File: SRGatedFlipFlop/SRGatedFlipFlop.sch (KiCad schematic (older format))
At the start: 5 parts, among them U1 74LS08, U2 74LS08, U3 74LS02, U4 74LS04

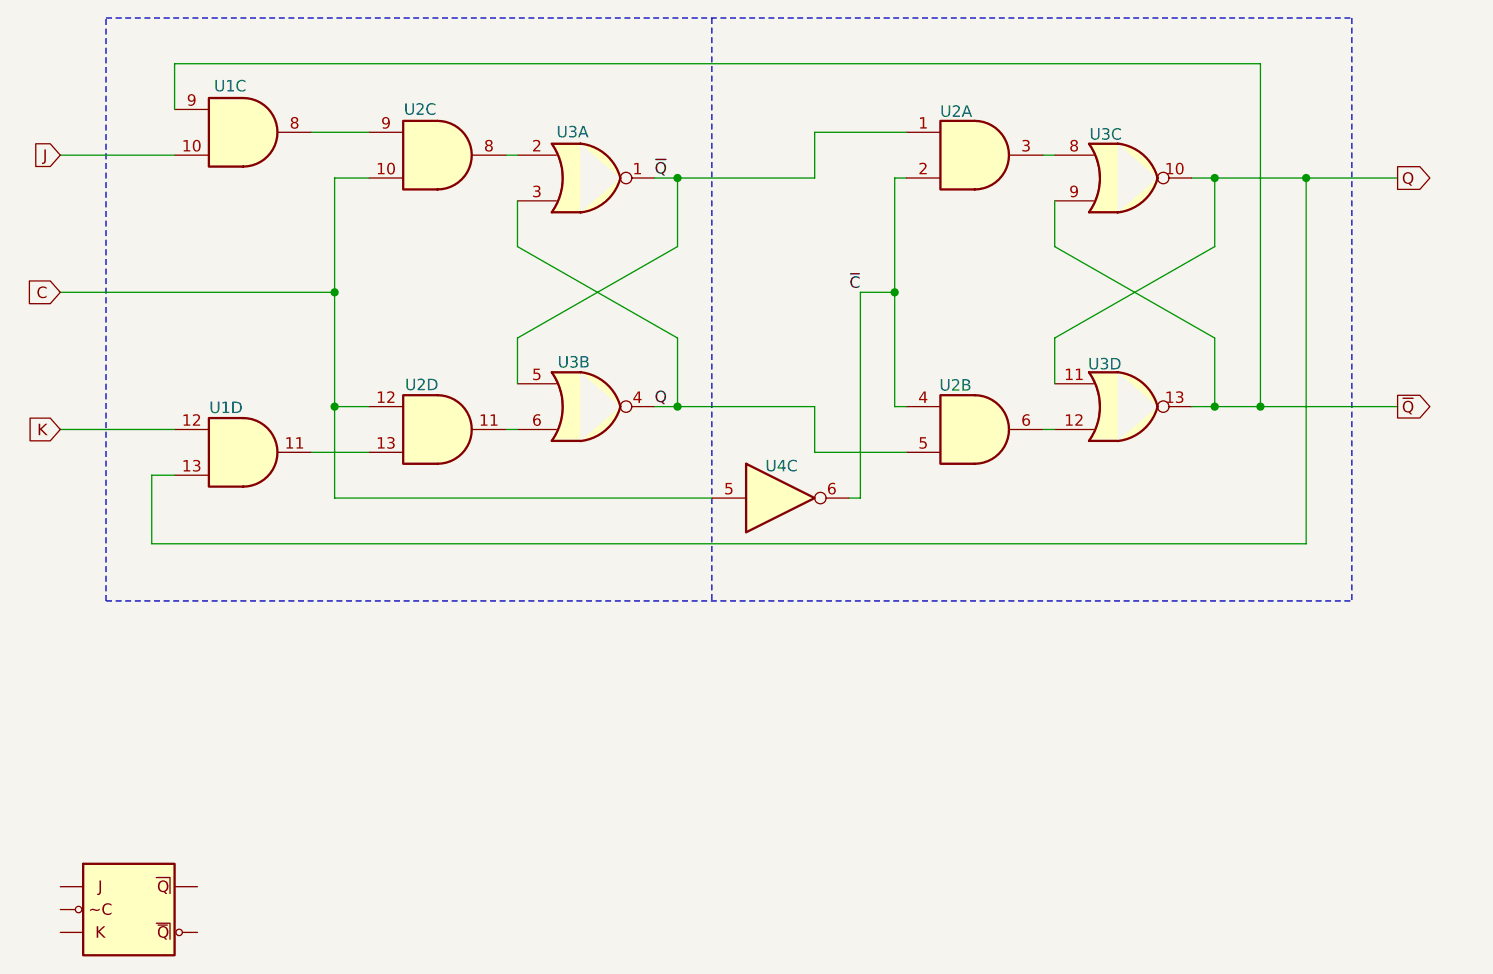
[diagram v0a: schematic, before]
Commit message: add gated S/R latch
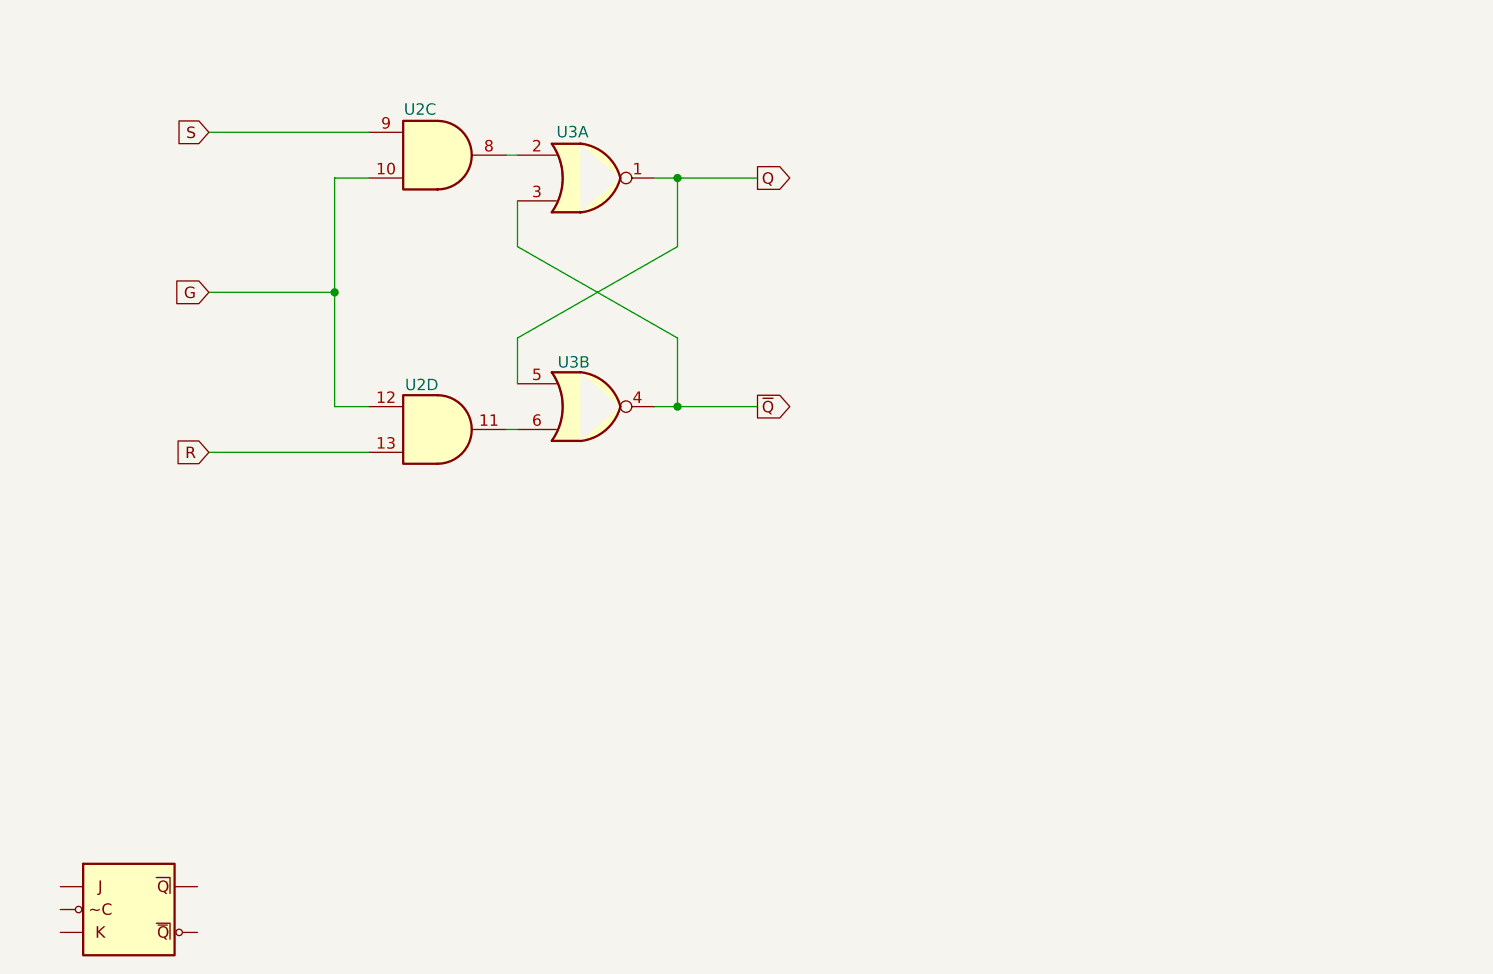
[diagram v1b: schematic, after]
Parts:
- removed U1: 74LS08, symbol 74xx:74LS08
- removed unit 2 of U2
- removed unit 1 of U2
- removed unit 4 of U3
- removed unit 3 of U3
- removed U4: 74LS04, symbol 74xx:74LS04
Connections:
- net Q: now also U3.1, U3.5; no longer U3.3, U3.4
- net ~Q: now also U3.3, U3.4; no longer U3.1, U3.5
- net S: now reaches U2.9
- net R: now reaches U2.13
- net C renamed G
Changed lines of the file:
@@
 EESchema Schematic File Version 4
-LIBS:FlipFlops-cache
+LIBS:SRGatedFlipFlop-cache
 EELAYER 30 0
 EELAYER END
@@
 Wire Wire Line
 	5650 3950 5650 4250
-Connection ~ 5650 4250
 Wire Wire Line
 	5650 3250 5650 3550
 Wire Wire Line
 	5650 3550 4950 3950
-Connection ~ 5650 3250
-Wire Wire Line
-	5650 3250 6250 3250
-$Comp
-L 74xx:74LS04 U4
-U 3 1 5F9C789E
-P 6100 4650
-F 0 "U4" H 6105 4790 50  0000 C CNN
-F 1 "74LS04" H 6100 4900 50  0001 C CNN
-F 2 "" H 6100 4650 50  0001 C CNN
-F 3 "http://www.ti.com/lit/gpn/sn74LS04" H 6100 4650 50  0001 C CNN
-	3    6100 4650
-	1    0    0    -1
-$EndComp
-Wire Wire Line
-	6450 3750 6450 4650
-Wire Wire Line
-	6450 4650 6400 4650
-Wire Wire Line
-	6450 3750 6600 3750
-Wire Wire Line
-	8200 4250 8200 2750
-Wire Wire Line
-	8400 3250 8400 4850
-Wire Wire Line
-	8400 4850 3350 4850
-Wire Wire Line
-	3450 4350 2950 4350
-Wire Wire Line
-	3450 4550 3350 4550
-Wire Wire Line
-	3350 4550 3350 4850
-Wire Notes Line
-	5800 2550 5800 5100
-Wire Notes Line
-	3150 5100 3150 2550
-Wire Notes Line
-	8600 2550 8600 5100
-Wire Notes Line
-	3150 5100 8600 5100
-Wire Notes Line
-	3150 2550 8600 2550
-Wire Wire Line
-	8200 2750 3450 2750
-Wire Wire Line
-	3450 3150 2950 3150
-Wire Wire Line
-	3450 2750 3450 2950
-$Comp
-L 74xx:74LS08 U1
-U 3 1 5F9D19F8
-P 3750 3050
-F 0 "U1" H 3693 3252 50  0000 C CNN
-F 1 "74LS08" H 3750 3300 50  0001 C CNN
-F 2 "" H 3750 3050 50  0001 C CNN
-F 3 "http://www.ti.com/lit/gpn/sn74LS08" H 3750 3050 50  0001 C CNN
-	3    3750 3050
-	1    0    0    -1
-$EndComp
 Connection ~ 4150 3750
 Wire Wire Line
@@
 Wire Wire Line
 	4150 3250 4150 3750
-Wire Wire Line
-	4300 3050 4050 3050
 $Comp
 L 74xx:74LS08 U2
@@
 	1    0    0    -1
 $EndComp
-$Comp
-L 74xx:74LS08 U1
-U 4 1 5F9CF647
-P 3750 4450
-F 0 "U1" H 3675 4645 50  0000 C CNN
-F 1 "74LS08" H 3750 4700 50  0001 C CNN
-F 2 "" H 3750 4450 50  0001 C CNN
-F 3 "http://www.ti.com/lit/gpn/sn74LS08" H 3750 4450 50  0001 C CNN
-	4    3750 4450
-	1    0    0    -1
-$EndComp
 Wire Wire Line
-	2950 3750 4150 3750
-Wire Wire Line
-	4150 4650 5800 4650
-Wire Wire Line
-	4050 4450 4300 4450
+	3600 3750 4150 3750
 Wire Wire Line
 	4300 3250 4150 3250
 Wire Wire Line
 	4300 4250 4150 4250
-Wire Wire Line
-	4150 4650 4150 4250
-Connection ~ 4150 4250
-$Comp
-L 74xx:74LS02 U3
-U 4 1 5FA5F768
-P 7600 4250
-F 0 "U3" H 7519 4436 50  0000 C CNN
-F 1 "74LS02" H 7600 4500 50  0001 C CNN
-F 2 "" H 7600 4250 50  0001 C CNN
-F 3 "http://www.ti.com/lit/gpn/sn74ls02" H 7600 4250 50  0001 C CNN
-	4    7600 4250
-	1    0    0    -1
-$EndComp
-Wire Wire Line
-	7900 3250 8000 3250
-Wire Wire Line
-	7900 4250 8000 4250
-Wire Wire Line
-	7300 3550 7300 3350
-Wire Wire Line
-	7300 4150 7300 3950
-Wire Wire Line
-	7300 3550 8000 3950
-Wire Wire Line
-	8000 3950 8000 4250
-Connection ~ 8000 4250
-Wire Wire Line
-	8000 3250 8000 3550
-Wire Wire Line
-	8000 3550 7300 3950
-Connection ~ 8000 3250
-Wire Wire Line
-	8000 3250 8400 3250
-Wire Wire Line
-	7250 4350 7300 4350
-$Comp
-L 74xx:74LS08 U2
-U 2 1 5FA5F77B
-P 6950 4350
-F 0 "U2" H 6866 4543 50  0000 C CNN
-F 1 "74LS08" H 6950 4600 50  0001 C CNN
-F 2 "" H 6950 4350 50  0001 C CNN
-F 3 "http://www.ti.com/lit/gpn/sn74LS08" H 6950 4350 50  0001 C CNN
-	2    6950 4350
-	1    0    0    -1
-$EndComp
-Wire Wire Line
-	7250 3150 7300 3150
-$Comp
-L 74xx:74LS08 U2
-U 1 1 5FA5F783
-P 6950 3150
-F 0 "U2" H 6869 3341 50  0000 C CNN
-F 1 "74LS08" H 6950 3400 50  0001 C CNN
-F 2 "" H 6950 3150 50  0001 C CNN
-F 3 "http://www.ti.com/lit/gpn/sn74LS08" H 6950 3150 50  0001 C CNN
-	1    6950 3150
-	1    0    0    -1
-$EndComp
-$Comp
-L 74xx:74LS02 U3
-U 3 1 5FA5F789
-P 7600 3250
-F 0 "U3" H 7523 3441 50  0000 C CNN
-F 1 "74LS02" H 7600 3500 50  0001 C CNN
-F 2 "" H 7600 3250 50  0001 C CNN
-F 3 "http://www.ti.com/lit/gpn/sn74ls02" H 7600 3250 50  0001 C CNN
-	3    7600 3250
-	1    0    0    -1
-$EndComp
-Wire Wire Line
-	6650 3250 6600 3250
-Wire Wire Line
-	8000 4250 8200 4250
-Wire Wire Line
-	8400 3250 8800 3250
-Connection ~ 8400 3250
-Wire Wire Line
-	8200 4250 8800 4250
-Connection ~ 8200 4250
-Wire Wire Line
-	6650 4250 6600 4250
-Wire Wire Line
-	5650 4250 6250 4250
-Wire Wire Line
-	6250 3250 6250 3050
-Wire Wire Line
-	6250 3050 6650 3050
-Wire Wire Line
-	6250 4450 6650 4450
-Wire Wire Line
-	6250 4250 6250 4450
-Wire Wire Line
-	6600 3750 6600 3250
-Wire Wire Line
-	6600 3750 6600 4250
-Connection ~ 6600 3750
-Text GLabel 2950 3150 0    50   Input ~ 0
-J
-Text GLabel 2950 3750 0    50   Input ~ 0
-C
-Text GLabel 2950 4350 0    50   Input ~ 0
-K
-Text GLabel 8800 3250 2    50   Output ~ 0
+Text GLabel 3600 3050 0    50   Input ~ 0
+S
+Text GLabel 3600 3750 0    50   Input ~ 0
+G
+Text GLabel 3600 4450 0    50   Input ~ 0
+R
+Text GLabel 6000 3250 2    50   Output ~ 0
 Q
-Text GLabel 8800 4250 2    50   Output ~ 0
+Text GLabel 6000 4250 2    50   Output ~ 0
 ~Q
-Text Label 6450 3750 2    50   ~ 0
-~C
-Text Label 5550 3250 0    50   ~ 0
-~Q
-Text Label 5550 4250 0    50   ~ 0
-Q
 $Comp
 L 00TJR:JK_MS U?
@@
 	1    0    0    -1
 $EndComp
+Wire Wire Line
+	3600 3050 4300 3050
+Wire Wire Line
+	3600 4450 4300 4450
+Wire Wire Line
+	5650 3250 6000 3250
+Connection ~ 5650 3250
+Wire Wire Line
+	5650 4250 6000 4250
+Connection ~ 5650 4250
 $EndSCHEMATC
